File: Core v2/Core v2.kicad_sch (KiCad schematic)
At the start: 49 parts, among them CN1 PJ-3200, J1 Serial Debug, J2 USB_C_Receptacle_USB2.0, Q1 BSS138, SW1 SW_SPST, SW2 SW_SPST, SW3 SW_SPST, U1 DL-TX1-433M, U2 H34B-433M, U3 ESP32-S3-WROOM-1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

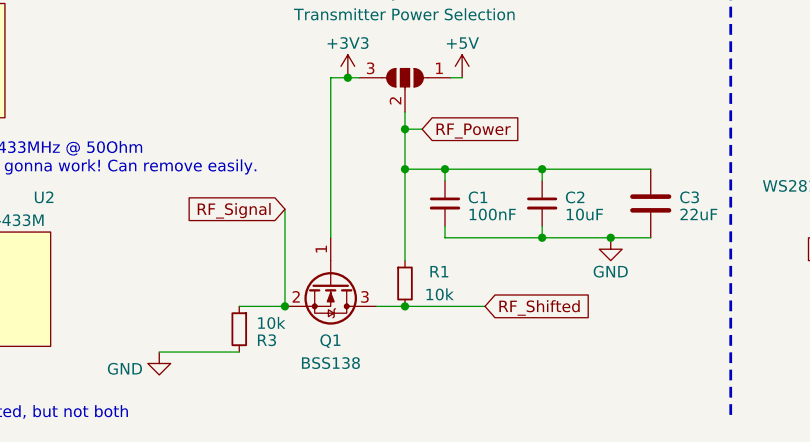
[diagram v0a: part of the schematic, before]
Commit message: Remove R1 from Core V2.0 BOM/CPL
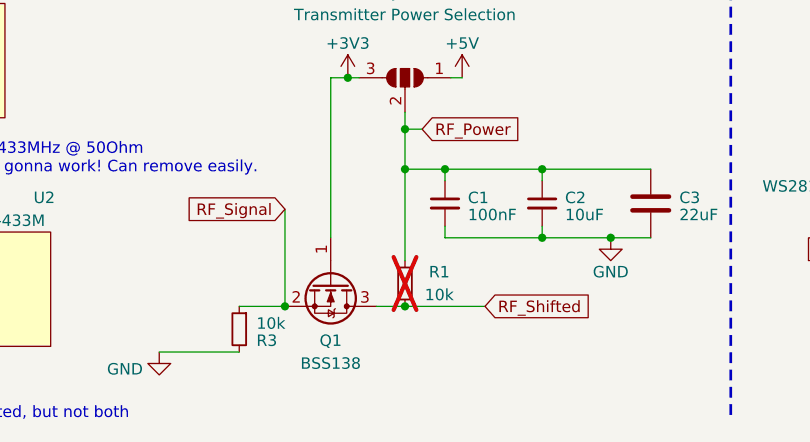
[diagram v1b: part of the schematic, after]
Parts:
- R1: now not fitted
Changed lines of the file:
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@@
   )
   (symbol (lib_id "Device:R_Small") (at 95.885 182.245 0) (unit 1)
-    (in_bom yes) (on_board yes) (dnp no)
+    (in_bom yes) (on_board yes) (dnp yes)
     (property "Reference" "R1" (at 99.695 180.975 0)
       (effects (font (size 1.27 1.27)))

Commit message: Core V2.1 KiCad + JLC Files
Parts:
- added C13: 100nF, Capacitor_SMD:C_0603_1608Metric_Pad1.08x0.95mm_HandSolder, symbol Device:C_Small
- added L1, L2: L, Inductor_SMD:L_0603_1608Metric_Pad1.05x0.95mm_HandSolder, symbol Device:L
- AE1: footprint Connector_PinHeader_2.54mm:PinHeader_1x01_P2.54mm_Vertical -> Connector_Pin:Pin_D1.0mm_L10.0mm
- J1, JP1, JP2, JP3, R1, TP1, TP2, TP3, TP4, TP5, TP6: now left out of the parts list
- U4: now not fitted; now left out of the parts list
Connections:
- net +3V3: now also JP1.1 (A); no longer JP1.3 (B)
- net +5V: now also JP1.3 (B); no longer JP1.1 (A)
- net EN: now also C13.1
- net GND: now also C13.2, L1.2, L2.2
- net at C12.2, U1.4 (ANT), U2.1 (ANT): now also L2.1
- net at AE1.1 (A), C12.1: now also L1.1
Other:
- note added: "C12 - 73pF DC Bypass for 433MHz @ 50Ohm"
- note added: "OpenShock Core V2.1"
- note added: "PSRAM variants are not required for OpenShock firmware usage. 8MB Flash variant preferred."
- note added: "R1 DNP'd to avoid unwanted transmissions when ESP is resetting/booting."
- note added: "TODO?: Maybe use 2 MOSFETs for proper active high shifting?"
- note added: "Unpopulated Pi Network For future potential tuning"
- note removed: "Coupling for 433MHz @ 50Ohm No idea if it's gonna work! Can remove easily."
- note removed: "OpenShock Core V2"
- note removed: "PSRAM Variants are not required for OpenShock firmware usage."
- moved on the sheet: AE1, C1, C12, C2, C3, D1, F1, J2, JP1, Q1, R1, R10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

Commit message: Core V2.2 KiCad + JLC Files
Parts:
- U5: value AMS1117-3.3 -> AP2114HA-3.3
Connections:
- net +3V3: now also U5.3 (VO); no longer U5.2 (VO)
- net +5V: now also U5.1 (VI); no longer U5.3 (VI)
- net GND: now also U5.2 (GND); no longer U5.1 (GND)
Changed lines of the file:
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@@
 			)
 		)
-		(property "Value" "AMS1117-3.3"
+		(property "Value" "AP2114HA-3.3"
 			(at 262.255 109.855 0)
 			(effects
@@
 			)
 		)
-		(property "Datasheet" "http://www.advanced-monolithic.com/pdf/ds1117.pdf"
+		(property "Datasheet" "https://wmsc.lcsc.com/wmsc/upload/file/pdf/v2/lcsc/2304140030_Diodes-Incorporated-AP2114HA-3-3TRG1_C460314.pdf"
 			(at 264.795 120.015 0)
 			(effects
